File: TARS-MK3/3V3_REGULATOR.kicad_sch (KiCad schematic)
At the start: 16 parts, among them J1 Conn_02x12_Odd_Even, J2 Conn_02x12_Odd_Even, J3 Conn_02x12_Odd_Even, J4 Conn_02x12_Odd_Even, U1 ISS_SENSOR_SUITE_V_1, U2 Teensy4.1_bare, U3 LP2985-3.0

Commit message: Did schematic
Did schematic
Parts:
- removed BT1: CR1225, Battery:BatteryHolder_Keystone_3000_1x12mm, symbol Device:Battery_Cell
- removed D1, D2, D3, D4: LED, LED_SMD:LED_0805_2012Metric, symbol D24V50F5:LED
- removed R1, R2, R3, R4: 470, Resistor_SMD:R_0805_2012Metric, symbol D24V50F5:R_US
- removed U1: ISS_SENSOR_SUITE_V_1, Sensorsuite:General Sensor Module - 8x10 pin, symbol SensorModule:ISS_SENSOR_SUITE_V_1
- removed U2: Teensy4.1_bare, Teensy:Teensy41_bare, symbol Teensy:Teensy4.1_bare
- removed U3: LP2985-3.0, Package_TO_SOT_SMD:SOT-23-5, symbol Regulator_Linear:LP2985-3.0
- added Q101: DMG2302U, Package_TO_SOT_SMD:SOT-23, symbol Transistor_FET:DMG2302U
- added R101: 10K, Resistor_SMD:R_0805_2012Metric, symbol D24V50F5:R_Small_US
- added U101: D36V28F3, D36V28F3:D36V28F3, symbol D36V28F3:D36V28F3
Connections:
- net 3V3: now also Q101.2 (S)
- net GND: now also U101.3 (GND), U101.4 (GND)
- new net: Q101.3 (D), R101.2, U101.5 (OUT)
- new net EN: Q101.1 (G), R101.1, U101.1 (EN)
- new net IN: U101.2 (VIN)
- no-connect marks 0 -> 1
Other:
- note removed: "This LED is Blue not Green"
- note removed: "This LED is Green not Red"
- note removed: "This LED is White not Blue"

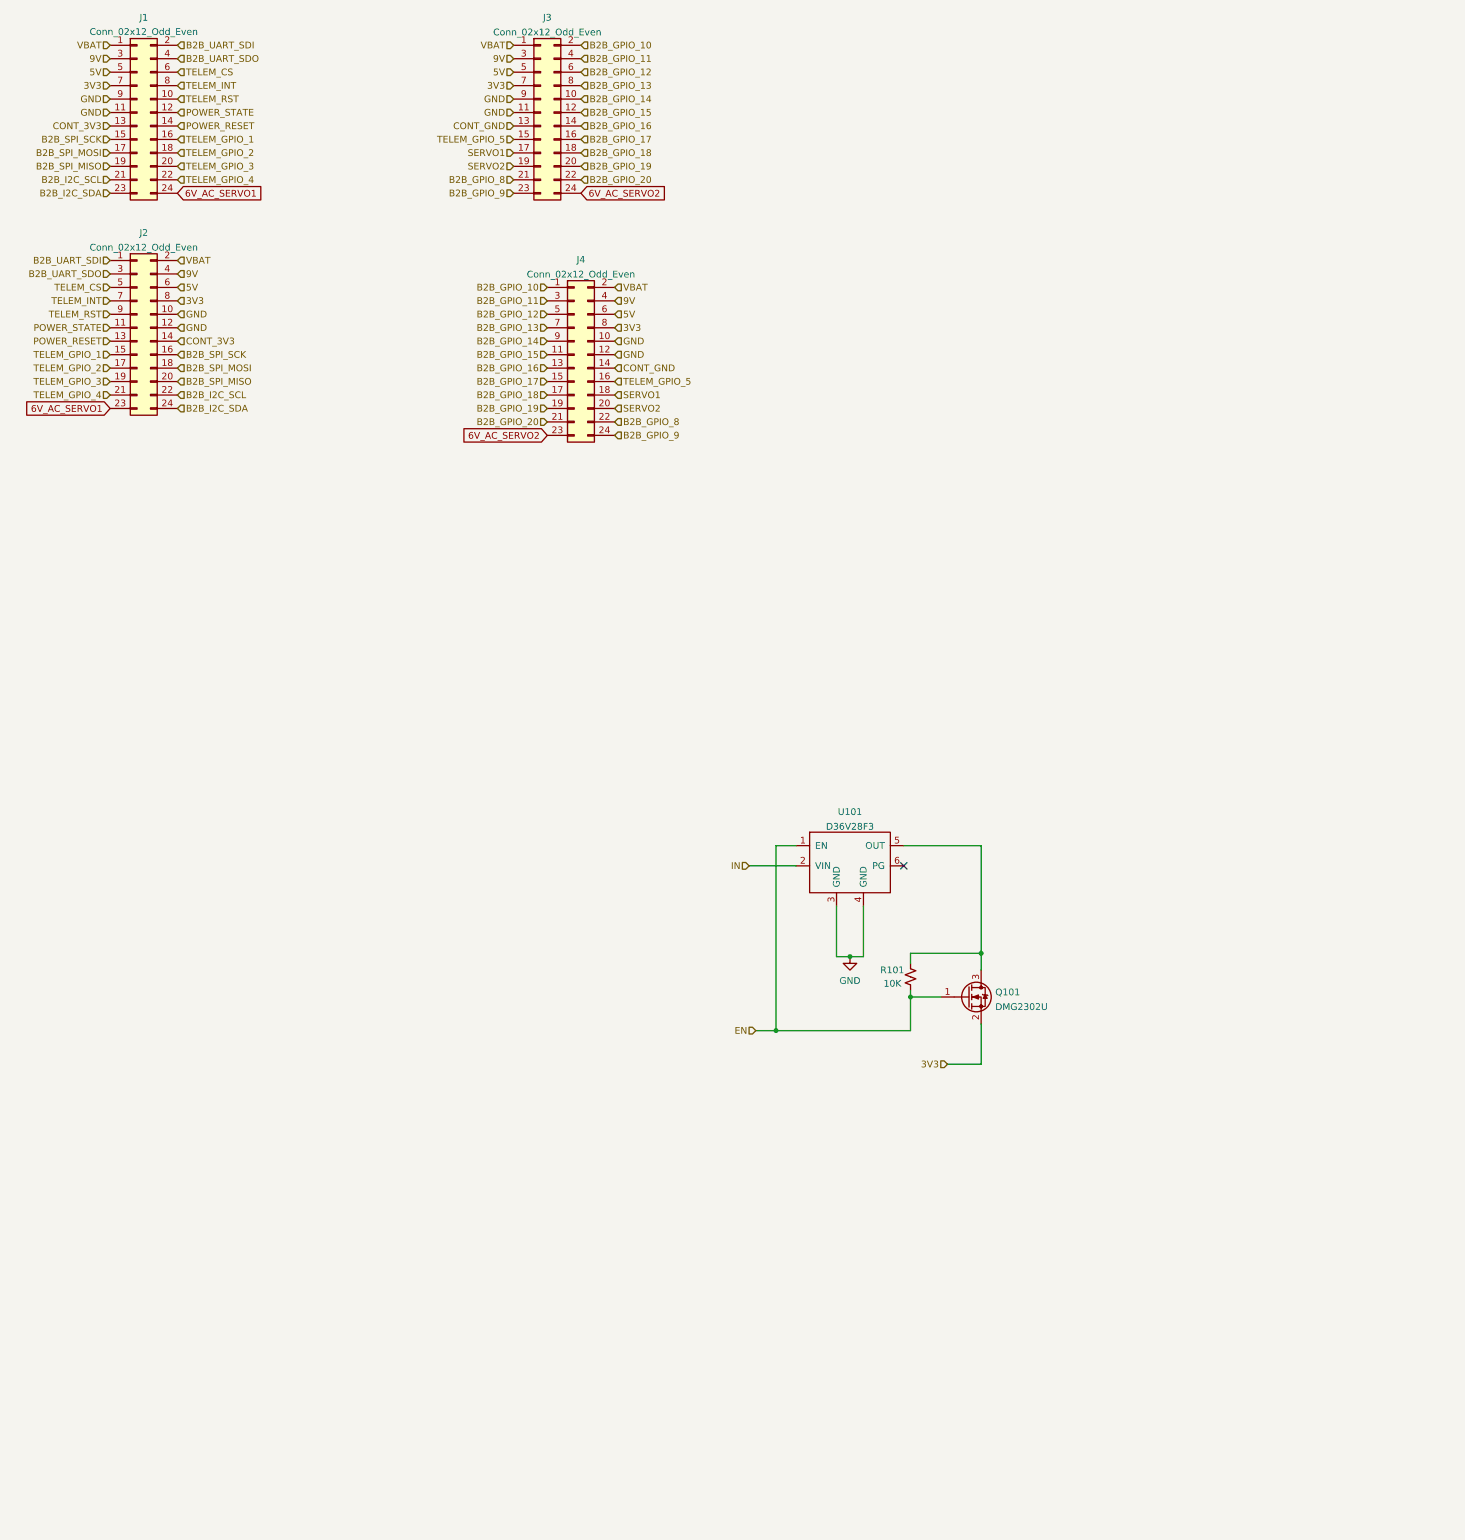
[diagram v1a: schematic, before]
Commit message: finished DIY 3.3V regulator
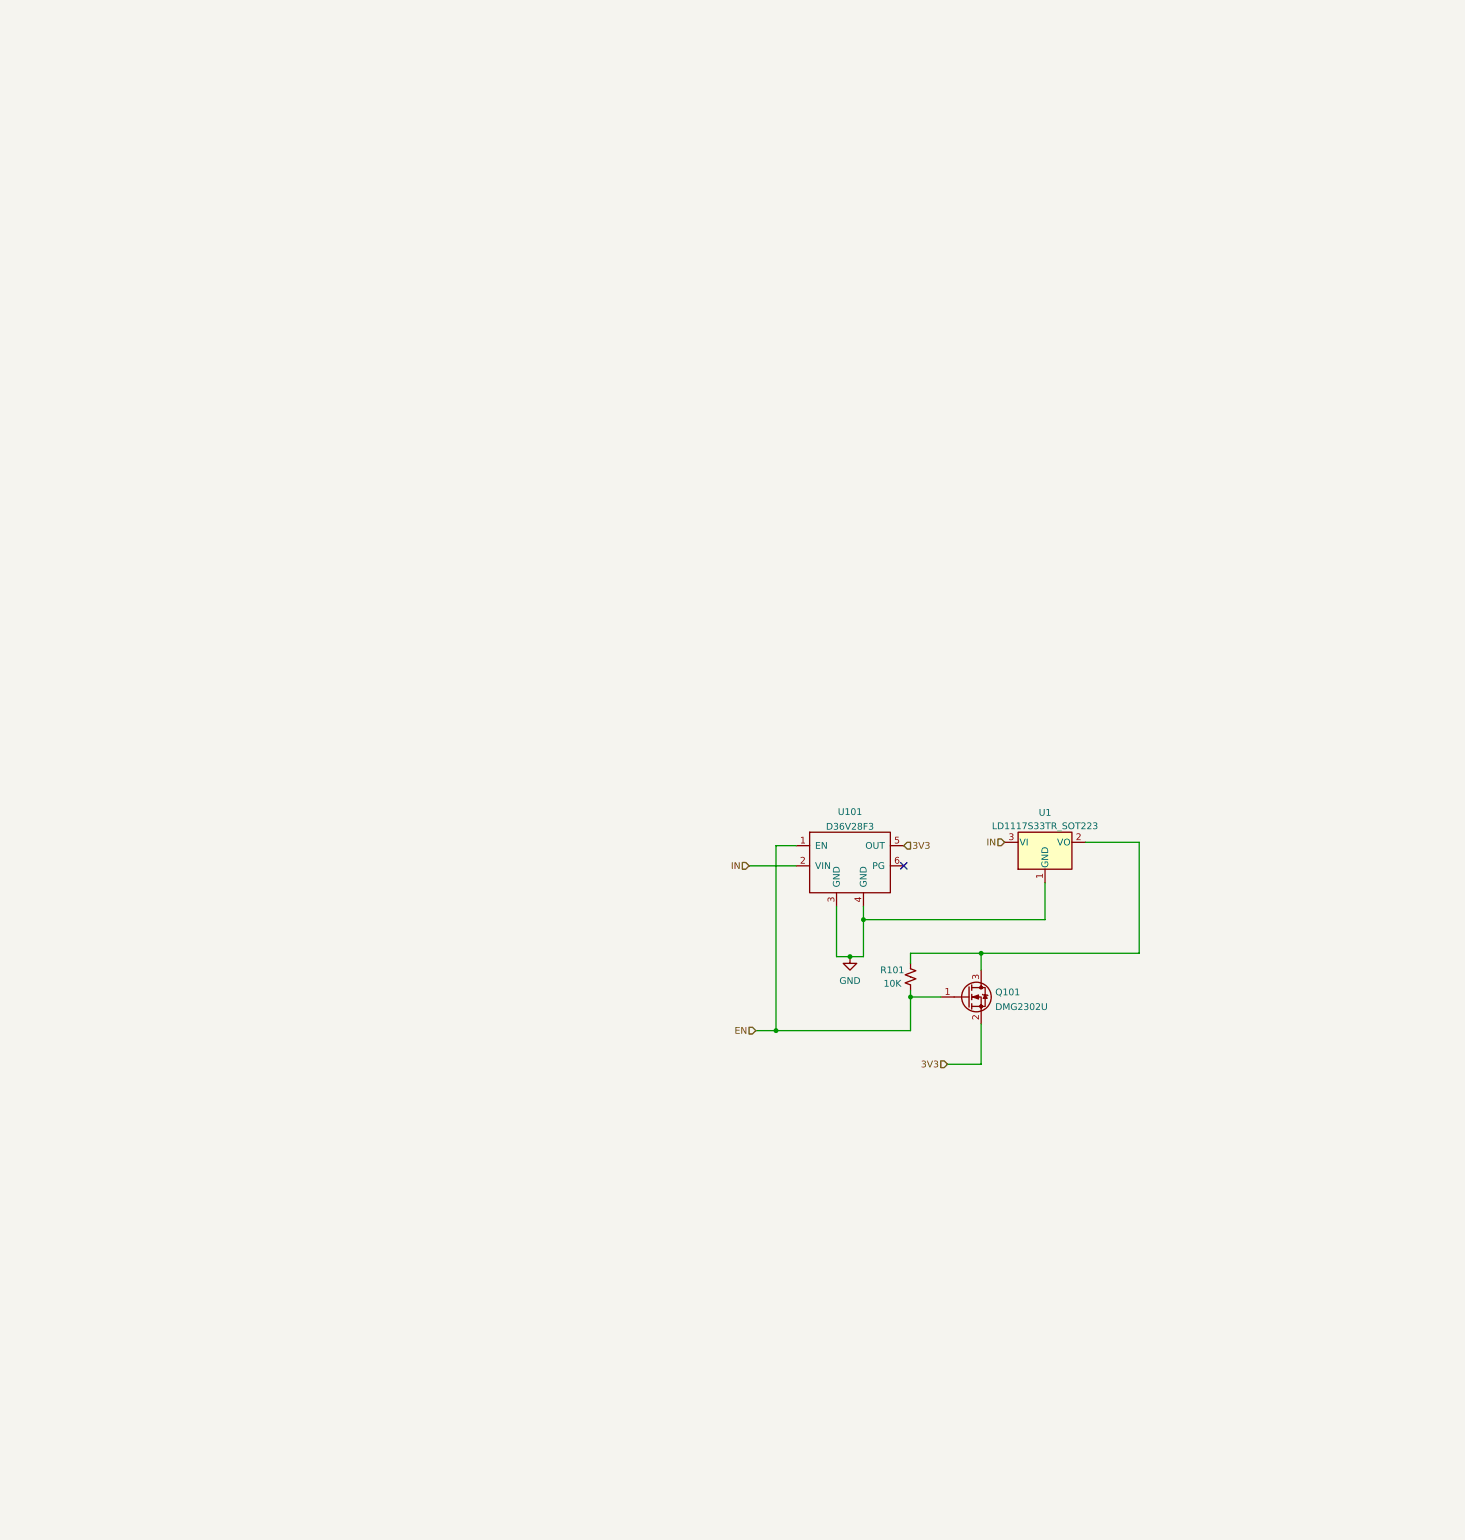
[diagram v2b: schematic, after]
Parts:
- removed J1, J2, J3, J4: Conn_02x12_Odd_Even, Connector_PinHeader_2.54mm:PinHeader_2x12_P2.54mm_Vertical_SMD, symbol Connector_Generic:Conn_02x12_Odd_Even
- added U1: LD1117S33TR_SOT223, Package_TO_SOT_SMD:SOT-223-3_TabPin2, symbol Regulator_Linear:LD1117S33TR_SOT223
- U101: footprint D36V28F3:D36V28F3 -> Pololu_regulators:Pololu_3V3_5V_9V
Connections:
- net 3V3: now also U101.5 (OUT)
- net GND: now also U1.1 (GND)
- net IN: now also U1.3 (VI)
- net at Q101.3 (D), R101.2: now also U1.2 (VO); no longer U101.5 (OUT)
